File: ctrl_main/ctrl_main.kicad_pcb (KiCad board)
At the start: 2 copper layers, 53.3 x 101.6 mm, 19 parts, among them IC1 SN74HC125N, J1 B2B-XH-A(LF)(SN), J2 B2B-XH-A(LF)(SN), J3 B2B-XH-A(LF)(SN), P10 CONN_01X04, P11 CONN_01X03, P12 CONN_01X03, P4 CONN_01X04, P5 CONN_01X04, P6 CONN_01X04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

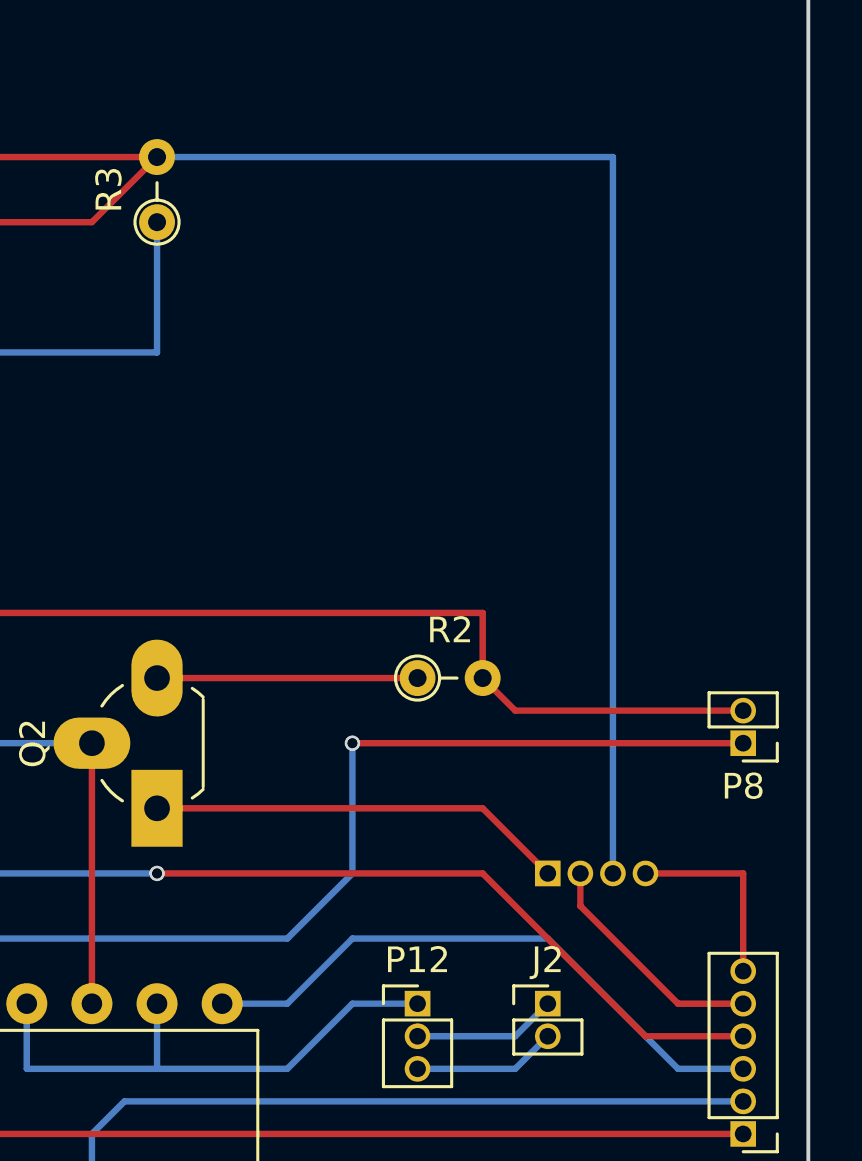
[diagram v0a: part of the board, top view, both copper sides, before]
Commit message: 測定系との通信コネクタを4p->3pに変更（5Vを削除）
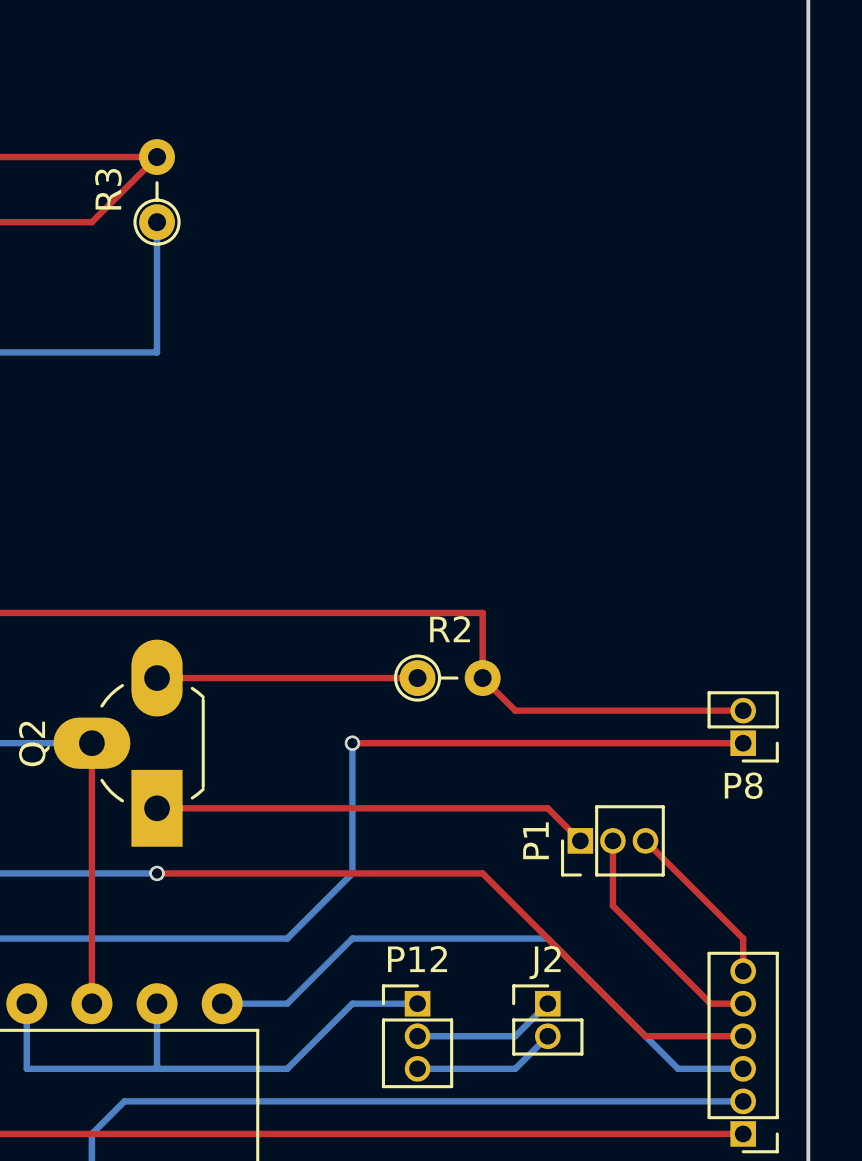
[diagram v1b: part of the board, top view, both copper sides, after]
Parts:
- removed P10: CONN_01X04, Pin_Headers:Pin_Header_Straight_1x04_Pitch1.27mm
- added P1: CONN_01X03, Pin_Headers:Pin_Header_Straight_1x03_Pitch1.27mm, F.Cu at (210.8, 87.6)
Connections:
- P8 pad 2: Net-(IC1-Pad13) -> Net-(IC1-Pad10)
- Q2 pad 2: Net-(IC1-Pad10) -> Net-(IC1-Pad13)
- R2 pad 2: Net-(IC1-Pad13) -> Net-(IC1-Pad10)
- R4 pad 1: Net-(IC1-Pad10) -> Net-(IC1-Pad13)
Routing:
- net 5V: track 157.0 -> 111.3 mm
- net Net-(IC1-Pad13): track 49.8 -> 54.4 mm
- net Net-(IC1-Pad10): track 17.8 -> 13.2 mm
- net Net-(P1-Pad3): track 7.62 -> 6.66 mm
- net CTRLGND: track 145.2 -> 145.9 mm
